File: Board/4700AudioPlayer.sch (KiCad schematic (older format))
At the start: 19 parts, among them U1 74HC164, U10 74HC74, U11 74HC04, U12 74HC590, U13 23K256-I_SN, U14 74LS157, U15 74HC595, U16 23K256-I_SN, U2 74HC164, U3 74HC164, U4 74HC164, U5 74HC40103, U6 74HC40103, U7 74HC40103, U8 74HC40103, U9 74LS10

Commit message: [Wave] First version
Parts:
- removed U?: 74LS08, symbol 74xx:74LS08
- added U?: 74LS10, symbol 4xxx:4072
- added U? (x2): 74LS10, symbol 74xx:74LS10
- U? (x2): value 74LS08 -> 74LS10
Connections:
- net labels added: n_playback_end
- wire segments 243 -> 252
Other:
- note removed: ">"
- note removed: "Count 44 bytes\n(wave header)."
- note removed: "Mask clock until data\ncan be fetched from RAM."
- note removed: "Receive bytes from RAM.\nMask output until sample_out_en is high."
- moved on the sheet: U1, U10A, U11B, U12, U13, U14, U15, U16, U2, U3, U4, U5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

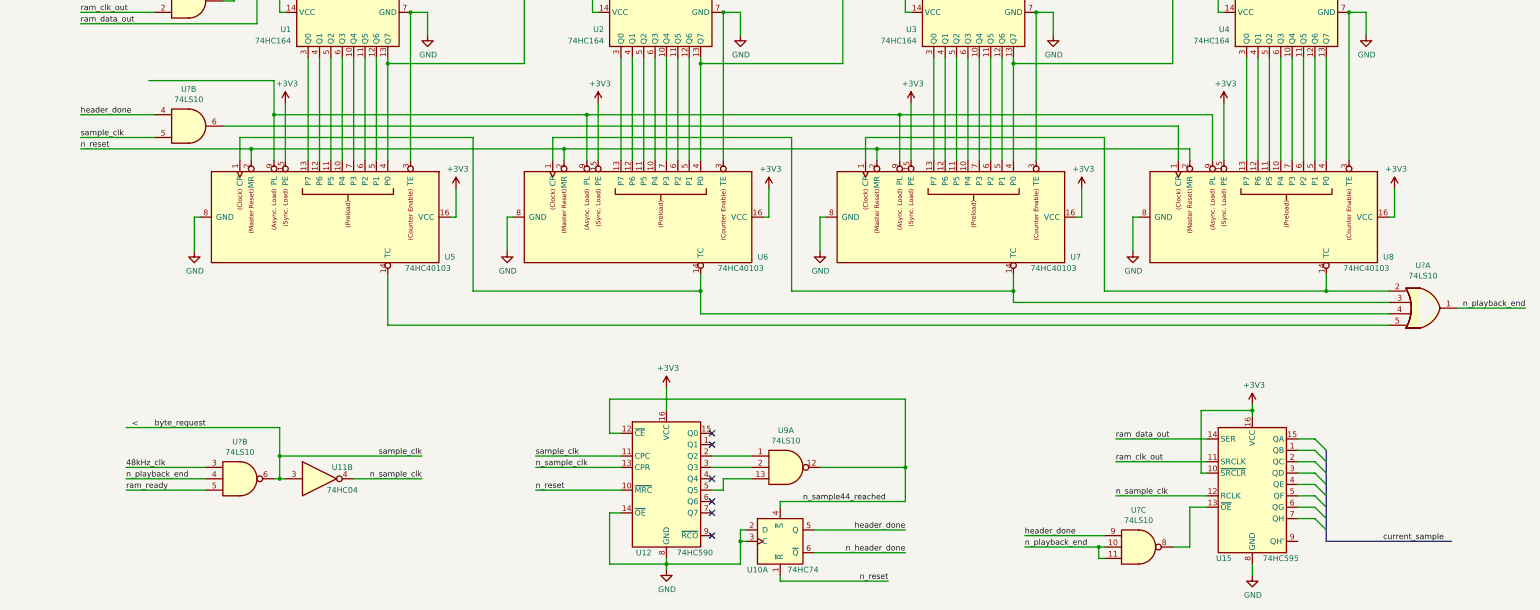
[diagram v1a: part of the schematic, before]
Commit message: [Wave] Fixed hangup after reset
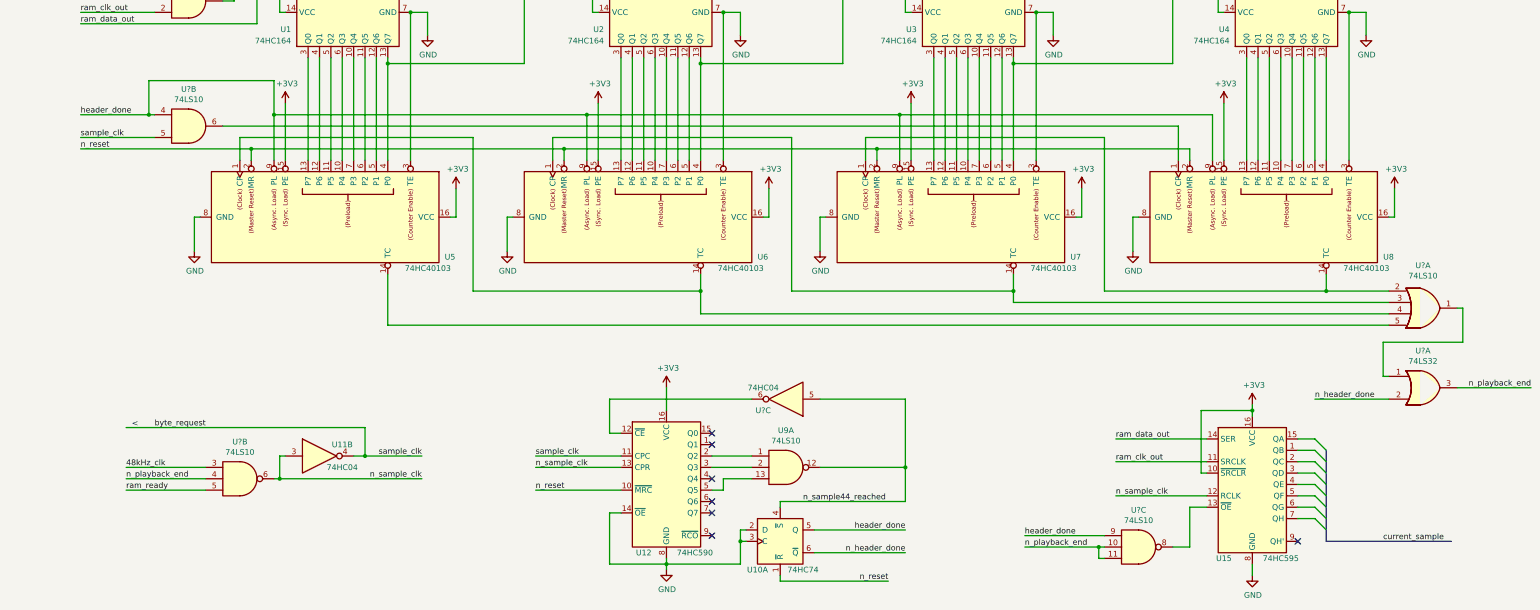
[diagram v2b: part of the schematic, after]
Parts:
- added U?: 74LS32, symbol 74xx:74LS32
- added U?: 74HC04, symbol 74xx:74HC04
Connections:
- net byte_request: now also U11.4; no longer U11.3, U?.6
- net header_done: now also U5.9 (PL), U6.9 (PL), U7.9 (PL), U8.9 (PL)
- net n_header_done: now also U?.2
- net n_playback_end: now also U?.3; no longer U?.1
- net n_sample44_reached: now also U?.5; no longer U12.12 (~CE)
- net n_sample_clk: now also U11.3, U?.6; no longer U11.4
- new net: U12.12 (~CE), U?.6
- new net: U?.1, U?.1
- no-connect marks 6 -> 7
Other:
- moved on the sheet: U11B
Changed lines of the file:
@@
 Wire Wire Line
 	8100 1950 8100 2150
-$Comp
-L My_74xx:74HC40103 U5
-U 1 1 60BDB6DC
-P 4550 3750
-F 0 "U5" V 4900 4700 50  0000 L CNN
-F 1 "74HC40103" V 5000 4350 50  0000 L CNN
-F 2 "Package_SO:SOIC-16_3.9x9.9mm_P1.27mm" H 4600 1850 50  0001 C CNN
-F 3 "https://www.ti.com/lit/ds/symlink/cd74hc40103.pdf" H 4600 1850 50  0001 C CNN
-	1    4550 3750
-	0    1    1    0
-$EndComp
 Wire Wire Line
 	5000 2350 5000 2400
@@
 header_done
 Wire Wire Line
-	4000 2850 4000 3250
-Wire Wire Line
 	5000 2400 5000 3250
 Connection ~ 5000 2400
@@
 	4600 2350 4600 3250
 Wire Wire Line
-	4500 2350 4500 3250
-Wire Wire Line
 	4400 2350 4400 3250
 Wire Wire Line
@@
 	4100 2750 4100 3250
 Wire Wire Line
-	4050 5850 5300 5850
-Wire Wire Line
-	4700 6050 5300 6050
-Wire Wire Line
-	11250 6650 11300 6650
-Connection ~ 11250 6650
-Wire Wire Line
-	11250 6750 11300 6750
-Wire Wire Line
-	11250 6650 11250 6750
-Text Label 10600 6650 0    50   ~ 0
-n_playback_end
-Wire Wire Line
-	10600 6650 11250 6650
-$Comp
-L 74xx:74LS10 U?
-U 3 1 6117C7C0
-P 11600 6650
-F 0 "U?" H 11600 6975 50  0000 C CNN
-F 1 "74LS10" H 11600 6884 50  0000 C CNN
-F 2 "" H 11600 6650 50  0001 C CNN
-F 3 "http://www.ti.com/lit/gpn/sn74LS10" H 11600 6650 50  0001 C CNN
-	3    11600 6650
-	1    0    0    -1
-$EndComp
+	4050 5850 4100 5850
 Wire Wire Line
 	2700 6050 3400 6050
 Text Label 2700 6050 0    50   ~ 0
 n_playback_end
-Text Label 10600 6550 0    50   ~ 0
-header_done
-Wire Wire Line
-	11300 6550 10600 6550
-Wire Wire Line
-	12050 6300 12200 6300
-Wire Wire Line
-	12050 6650 12050 6300
-Wire Wire Line
-	11900 6650 12050 6650
 Text Label 9550 6500 2    50   ~ 0
 header_done
 Wire Wire Line
 	8750 6500 9550 6500
-Wire Wire Line
-	2700 5600 4050 5600
-Wire Wire Line
-	11400 6200 12200 6200
 Wire Wire Line
 	8450 6250 9550 6250
@@
 n_header_done
 Wire Wire Line
-	6950 5350 9550 5350
+	6950 5350 8200 5350
 Connection ~ 9550 5950
 Wire Wire Line
@@
 Wire Wire Line
 	6950 6800 7450 6800
-Wire Wire Line
-	4050 6050 4100 6050
 Text Label 6300 6150 0    50   ~ 0
 n_reset
@@
 L 74xx:74HC04 U11
 U 2 1 60D35307
-P 4400 6050
-F 0 "U11" H 4600 6150 50  0000 C CNN
-F 1 "74HC04" H 4600 5950 50  0000 C CNN
-F 2 "" H 4400 6050 50  0001 C CNN
-F 3 "https://assets.nexperia.com/documents/data-sheet/74HC_HCT04.pdf" H 4400 6050 50  0001 C CNN
-	2    4400 6050
+P 4400 5850
+F 0 "U11" H 4600 5950 50  0000 C CNN
+F 1 "74HC04" H 4600 5750 50  0000 C CNN
+F 2 "" H 4400 5850 50  0001 C CNN
+F 3 "https://assets.nexperia.com/documents/data-sheet/74HC_HCT04.pdf" H 4400 5850 50  0001 C CNN
+	2    4400 5850
 	1    0    0    -1
 $EndComp
@@
 	11400 5900 12200 5900
 Wire Wire Line
-	12150 6000 12150 5450
-Wire Wire Line
-	12200 6000 12150 6000
-Wire Wire Line
 	12600 5450 12600 5500
 Connection ~ 12600 5450
-Wire Wire Line
-	12600 5450 12150 5450
 Wire Wire Line
 	12600 6800 12600 6900
@@
 n_sample_clk
 Wire Wire Line
-	4050 5600 4050 5850
-Connection ~ 4050 5850
-Wire Wire Line
 	2300 1750 2950 1750
 Text Label 2300 1150 0    50   ~ 0
@@
 	4000 2550 4000 2850
 Wire Wire Line
-	2300 2850 2950 2850
-Text Label 15000 4550 2    50   ~ 0
+	2300 2850 2900 2850
+Text Label 15050 5250 2    50   ~ 0
 n_playback_end
-Wire Wire Line
-	15000 4550 14400 4550
-Wire Bus Line
-	13250 5800 13250 6600
+$Comp
+L 4xxx:4072 U?
+U 1 1 60FAC43A
+P 14100 4550
+F 0 "U?" H 14100 4925 50  0000 C CNN
+F 1 "74LS10" H 14100 4834 50  0000 C CNN
+F 2 "" H 14100 4550 50  0001 C CNN
+F 3 "http://www.ti.com/lit/gpn/sn74LS10" H 14100 4550 50  0001 C CNN
+	1    14100 4550
+	1    0    0    -1
+$EndComp
+Wire Wire Line
+	2900 2550 4000 2550
+Wire Wire Line
+	4000 2850 4000 3250
+Wire Wire Line
+	4500 2350 4500 3250
+$Comp
+L My_74xx:74HC40103 U5
+U 1 1 60BDB6DC
+P 4550 3750
+F 0 "U5" V 4900 4700 50  0000 L CNN
+F 1 "74HC40103" V 5000 4350 50  0000 L CNN
+F 2 "Package_SO:SOIC-16_3.9x9.9mm_P1.27mm" H 4600 1850 50  0001 C CNN
+F 3 "https://www.ti.com/lit/ds/symlink/cd74hc40103.pdf" H 4600 1850 50  0001 C CNN
+	1    4550 3750
+	0    1    1    0
+$EndComp
+Text Label 13150 5350 0    50   ~ 0
+n_header_done
+$Comp
+L 74xx:74LS32 U?
+U 1 1 60B605D7
+P 14100 5250
+F 0 "U?" H 14100 5575 50  0000 C CNN
+F 1 "74LS32" H 14100 5484 50  0000 C CNN
+F 2 "" H 14100 5250 50  0001 C CNN
+F 3 "http://www.ti.com/lit/gpn/sn74LS32" H 14100 5250 50  0001 C CNN
+	1    14100 5250
+	1    0    0    -1
+$EndComp
+Wire Wire Line
+	13150 5350 13800 5350
+Wire Wire Line
+	13800 5150 13750 5150
+Wire Wire Line
+	13750 5150 13750 4850
+Wire Wire Line
+	13750 4850 14450 4850
+Wire Wire Line
+	14450 4850 14450 4550
+Wire Wire Line
+	14450 4550 14400 4550
+Wire Wire Line
+	15050 5250 14400 5250
+Wire Wire Line
+	2900 2550 2900 2850
+Connection ~ 2900 2850
+Wire Wire Line
+	2900 2850 2950 2850
+Wire Wire Line
+	4700 5850 4800 5850
+Wire Wire Line
+	4050 6050 5300 6050
+Wire Wire Line
+	4800 5600 4800 5850
+Wire Wire Line
+	2700 5600 4800 5600
+Connection ~ 4800 5850
+Wire Wire Line
+	4800 5850 5300 5850
+$Comp
+L 74xx:74HC04 U?
+U 3 1 60B84E20
+P 8500 5350
+F 0 "U?" H 8700 5450 50  0000 C CNN
+F 1 "74HC04" H 8700 5250 50  0000 C CNN
+F 2 "" H 8500 5350 50  0001 C CNN
+F 3 "https://assets.nexperia.com/documents/data-sheet/74HC_HCT04.pdf" H 8500 5350 50  0001 C CNN
+	3    8500 5350
+	-1   0    0    1
+$EndComp
+Wire Wire Line
+	8800 5350 9550 5350
 $Comp
 L 74xx:74LS10 U?
@@
 $EndComp
 $Comp
-L 4xxx:4072 U?
-U 1 1 60FAC43A
-P 14100 4550
-F 0 "U?" H 14100 4925 50  0000 C CNN
-F 1 "74LS10" H 14100 4834 50  0000 C CNN
-F 2 "" H 14100 4550 50  0001 C CNN
-F 3 "http://www.ti.com/lit/gpn/sn74LS10" H 14100 4550 50  0001 C CNN
-	1    14100 4550
+L 74xx:74LS08 U?
+U 1 1 60BA7967
+P 3250 1850
+F 0 "U?" H 3250 2175 50  0000 C CNN
+F 1 "74LS10" H 3250 2084 50  0000 C CNN
+F 2 "" H 3250 1850 50  0001 C CNN
+F 3 "http://www.ti.com/lit/gpn/sn74LS10" H 3250 1850 50  0001 C CNN
+	1    3250 1850
 	1    0    0    -1
 $EndComp
@@
 	1    0    0    -1
 $EndComp
-$Comp
-L 74xx:74LS08 U?
-U 1 1 60BA7967
-P 3250 1850
-F 0 "U?" H 3250 2175 50  0000 C CNN
-F 1 "74LS10" H 3250 2084 50  0000 C CNN
-F 2 "" H 3250 1850 50  0001 C CNN
-F 3 "http://www.ti.com/lit/gpn/sn74LS10" H 3250 1850 50  0001 C CNN
-	1    3250 1850
-	1    0    0    -1
-$EndComp
-Wire Wire Line
-	2900 2550 4000 2550
+Wire Wire Line
+	11400 6200 12200 6200
+Wire Wire Line
+	12600 5450 12150 5450
+Wire Wire Line
+	12200 6000 12150 6000
+Wire Wire Line
+	12150 6000 12150 5450
+Wire Wire Line
+	12050 6300 12200 6300
+Wire Wire Line
+	11900 6650 12050 6650
+Wire Wire Line
+	12050 6650 12050 6300
+Wire Bus Line
+	13250 5800 13250 6600
+$Comp
+L 74xx:74LS10 U?
+U 3 1 6117C7C0
+P 11600 6650
+F 0 "U?" H 11600 6975 50  0000 C CNN
+F 1 "74LS10" H 11600 6884 50  0000 C CNN
+F 2 "" H 11600 6650 50  0001 C CNN
+F 3 "http://www.ti.com/lit/gpn/sn74LS10" H 11600 6650 50  0001 C CNN
+	3    11600 6650
+	1    0    0    -1
+$EndComp
+Wire Wire Line
+	11300 6550 10600 6550
+Text Label 10600 6550 0    50   ~ 0
+header_done
+Wire Wire Line
+	10600 6650 11250 6650
+Text Label 10600 6650 0    50   ~ 0
+n_playback_end
+Wire Wire Line
+	11250 6650 11250 6750
+Wire Wire Line
+	11250 6750 11300 6750
+Connection ~ 11250 6650
+Wire Wire Line
+	11250 6650 11300 6650
+NoConn ~ 13000 6600
 $EndSCHEMATC

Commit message: [Wave] Bigger sheet size
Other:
- moved on the sheet: U1, U10A, U11B, U12, U13, U14, U15, U16, U2, U3, U4, U5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

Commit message: [RAM] Added Flipflop for RAM selection
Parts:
- added U?: 74HC74, symbol 74xx:74HC74
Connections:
- net GND: no longer U15.8 (GND)
- net n_reset: now also U?.13 (~R)
- net ram_data_out: now also U14.4 (Za)
- net ram_ready: now also U?.9 (Q)
- new net n_ram_ready: U?.8 (~Q)
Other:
- moved on the sheet: U1, U10A, U11B, U12, U13, U14, U15, U16, U2, U3, U4, U5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

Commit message: [RAM] Added registers for setup commands, [Wave] Switched data to MSB first
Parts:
- added U? (x6): 74LS165, symbol 74xx:74LS165
- U: renamed from U?; value 74LS10 -> 4072
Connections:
- net +3V3: now also U5.8 (GND), U6.8 (GND), U7.8 (GND), U8.8 (GND), U?.11 (D0), U?.11 (D0), U?.11 (D0), U?.11 (D0), U?.12 (D1), U?.12 (D1), U?.16 (VCC), U?.16 (VCC), U?.16 (VCC), U?.16 (VCC), U?.16 (VCC), U?.16 (VCC), U?.5 (D6), U?.5 (D6); no longer U5.16 (VCC), U6.16 (VCC), U7.16 (VCC), U8.16 (VCC)
- net GND: now also U5.16 (VCC), U6.16 (VCC), U7.16 (VCC), U8.16 (VCC), U?.10 (DS), U?.10 (DS), U?.12 (D1), U?.12 (D1), U?.12 (D1), U?.12 (D1), U?.13 (D2), U?.13 (D2), U?.13 (D2), U?.13 (D2), U?.13 (D2), U?.13 (D2), U?.14 (D3), U?.14 (D3), U?.14 (D3), U?.14 (D3), U?.14 (D3), U?.14 (D3), U?.15 (~CE), U?.15 (~CE), U?.15 (~CE), U?.15 (~CE), U?.15 (~CE), U?.15 (~CE), U?.3 (D4), U?.3 (D4), U?.3 (D4), U?.3 (D4), U?.3 (D4), U?.3 (D4), U?.4 (D5), U?.4 (D5), U?.4 (D5), U?.4 (D5), U?.4 (D5), U?.4 (D5), U?.5 (D6), U?.5 (D6), U?.5 (D6), U?.5 (D6), U?.6 (D7), U?.6 (D7), U?.6 (D7), U?.6 (D7), U?.6 (D7), U?.6 (D7), U?.8 (GND), U?.8 (GND), U?.8 (GND), U?.8 (GND), U?.8 (GND), U?.8 (GND); no longer U5.8 (GND), U6.8 (GND), U7.8 (GND), U8.8 (GND)
- net ram_select: now also U?.11 (D0)
- net at U8.10 (P4): now also U4.10 (Q4); no longer U4.6 (Q3)
- net at U8.11 (P5): now also U4.11 (Q5); no longer U4.5 (Q2)
- net at U8.12 (P6): now also U4.12 (Q6); no longer U4.4 (Q1)
- net at U8.13 (P7): now also U4.13 (Q7); no longer U4.3 (Q0)
- net at U8.4 (P0): now also U4.3 (Q0); no longer U4.13 (Q7)
- net at U8.5 (P1): now also U4.4 (Q1); no longer U4.12 (Q6)
- net at U8.6 (P2): now also U4.5 (Q2); no longer U4.11 (Q5)
- net at U8.7 (P3): now also U4.6 (Q3); no longer U4.10 (Q4)
- net at U3.13 (Q7), U4.1 (DSA), U4.2 (DSB): now also U7.13 (P7); no longer U7.4 (P0)
- net at U7.10 (P4): now also U3.10 (Q4); no longer U3.6 (Q3)
- net at U7.11 (P5): now also U3.11 (Q5); no longer U3.5 (Q2)
- net at U7.12 (P6): now also U3.12 (Q6); no longer U3.4 (Q1)
- net at U3.3 (Q0): now also U7.4 (P0); no longer U7.13 (P7)
- net at U7.5 (P1): now also U3.4 (Q1); no longer U3.12 (Q6)
- net at U7.6 (P2): now also U3.5 (Q2); no longer U3.11 (Q5)
- net at U7.7 (P3): now also U3.6 (Q3); no longer U3.10 (Q4)
- net at U2.13 (Q7), U3.1 (DSA), U3.2 (DSB): now also U6.13 (P7); no longer U6.4 (P0)
- net at U6.10 (P4): now also U2.10 (Q4); no longer U2.6 (Q3)
- net at U6.11 (P5): now also U2.11 (Q5); no longer U2.5 (Q2)
- net at U6.12 (P6): now also U2.12 (Q6); no longer U2.4 (Q1)
- net at U2.3 (Q0): now also U6.4 (P0); no longer U6.13 (P7)
- net at U6.5 (P1): now also U2.4 (Q1); no longer U2.12 (Q6)
- net at U6.6 (P2): now also U2.5 (Q2); no longer U2.11 (Q5)
- net at U6.7 (P3): now also U2.6 (Q3); no longer U2.10 (Q4)
- net at U1.13 (Q7), U2.1 (DSA), U2.2 (DSB): now also U5.13 (P7); no longer U5.4 (P0)
- net at U5.10 (P4): now also U1.10 (Q4); no longer U1.6 (Q3)
- net at U5.11 (P5): now also U1.11 (Q5); no longer U1.5 (Q2)
- net at U5.12 (P6): now also U1.12 (Q6); no longer U1.4 (Q1)
- net at U1.3 (Q0): now also U5.4 (P0); no longer U5.13 (P7)
- net at U5.5 (P1): now also U1.4 (Q1); no longer U1.12 (Q6)
- net at U5.6 (P2): now also U1.5 (Q2); no longer U1.11 (Q5)
- net at U5.7 (P3): now also U1.6 (Q3); no longer U1.10 (Q4)
- new net: U?.10 (DS), U?.9 (Q7) (x4)
- new net n_ram_select: U?.11 (D0)
- new net ram1_setup_clk: U?.2 (CP), U?.2 (CP), U?.2 (CP)
- new net ram1_setup_data: U?.9 (Q7)
- new net ram1_setup_init: U?.1 (~PL), U?.1 (~PL), U?.1 (~PL)
- new net ram2_setup_clk: U?.2 (CP), U?.2 (CP), U?.2 (CP)
- new net ram2_setup_data: U?.9 (Q7)
- new net ram2_setup_init: U?.1 (~PL), U?.1 (~PL), U?.1 (~PL)
- no-connect marks 7 -> 13
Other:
- note added: "Read / Write"
- note added: "Seq. mode, no hold"
- note added: "Write status reg."
- note added: "todo: maybe\ncheck for zeros \nas well"
- moved on the sheet: U1, U10A, U11B, U12, U13, U14, U15, U16, U2, U3, U4, U5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
